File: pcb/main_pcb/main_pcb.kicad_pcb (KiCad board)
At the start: 2 copper layers, 80 x 100 mm, 58 parts, among them J1 Conn_01x05, J10 Conn_01x06_Male, J11 Conn_01x04, J12 Screw_Terminal_01x02, J13 Conn_01x02_Male, J2 Conn_01x05, J3 Conn_01x05, J4 Conn_01x05, J5 Conn_01x05, J6 Conn_01x05, J7 Conn_01x04, J8 Conn_01x06_Male, J9 Conn_01x04, Q1 Q_PMOS_GDS, SW1 SW_SPDT, U1 LSM6DSO, U2 Teensy_4.1, U3 DRV8833, U4 LM1117-3.3, U5 TPIC74101

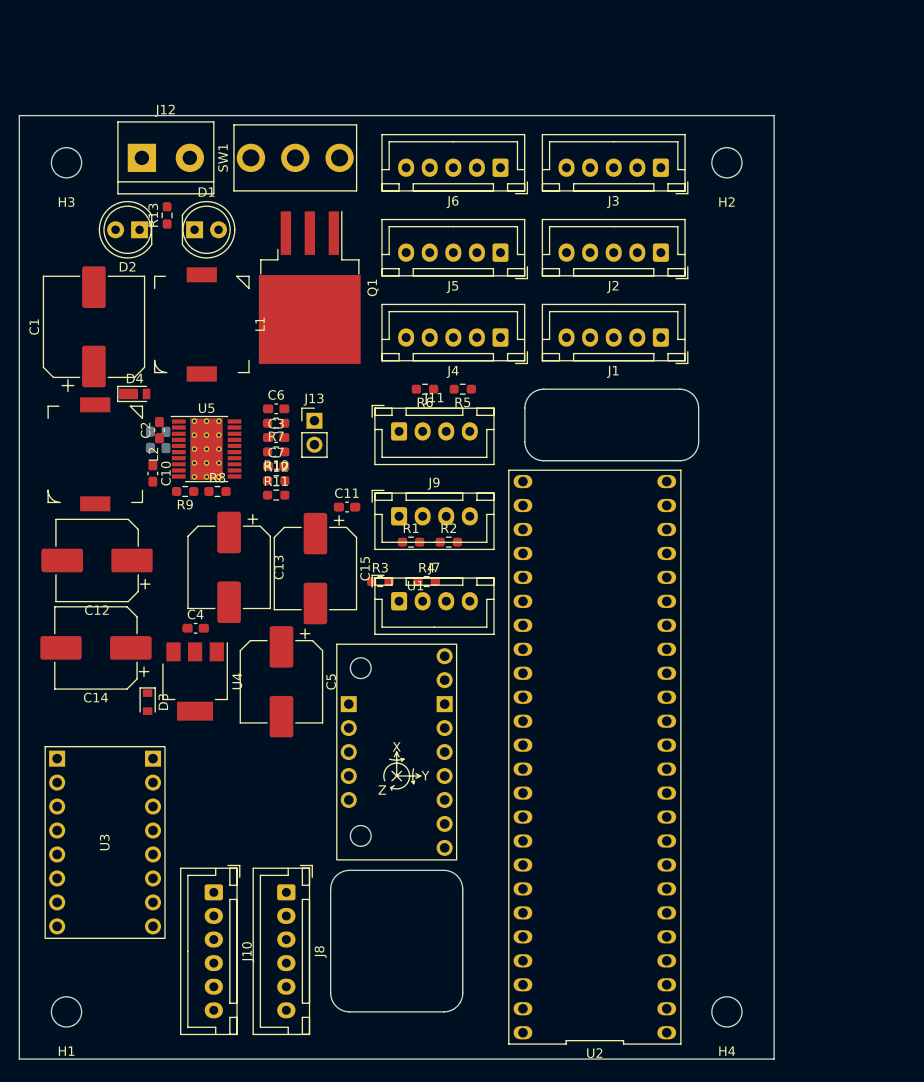
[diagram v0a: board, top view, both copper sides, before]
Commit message: Reorganize Teensy connections for optimized routing
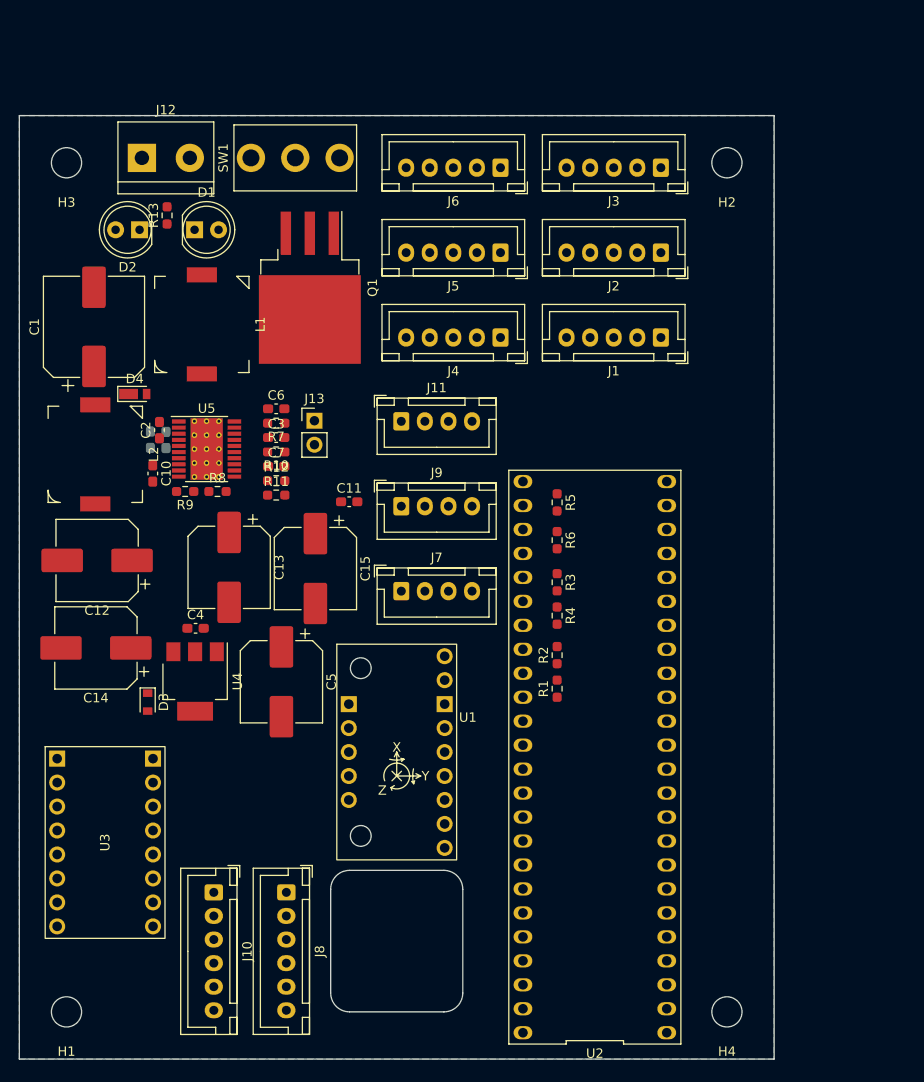
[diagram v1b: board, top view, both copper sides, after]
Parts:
- moved R1 21.9 mm to (107.0, 110.7), turned to 90 degrees
- moved R6 21.3 mm to (107.0, 95.0), turned to -90 degrees
- moved R3 18.7 mm to (107.0, 99.5), turned to -90 degrees
- moved R2 16.6 mm to (107.0, 107.2), turned to 90 degrees
- moved R5 15.6 mm to (107.0, 91.0), turned to -90 degrees
- moved R4 14.3 mm to (107.0, 103.0), turned to -90 degrees
- moved J11 1.09 mm to (90.5, 82.4)
- moved J7 1.09 mm to (90.5, 100.4)
- moved J9 1.09 mm to (90.5, 91.4)
- moved C11 0.60 mm to (85.0, 90.9)
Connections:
- net Net-(J2-Pad4) renamed /microcontroller/LCS2
- net Net-(J5-Pad4) renamed /microcontroller/LCS5
- J1 pad 2: /microcontroller/SDA -> /microcontroller/SDA2
- J1 pad 3: /microcontroller/SCL -> /microcontroller/SCL2
- J1 pad 4: Net-(J1-Pad4) -> /microcontroller/LCS1
- J2 pad 2: /microcontroller/SDA -> /microcontroller/SDA2
- J2 pad 3: /microcontroller/SCL -> /microcontroller/SCL2
- J3 pad 2: /microcontroller/SDA -> /microcontroller/SDA2
- J3 pad 3: /microcontroller/SCL -> /microcontroller/SCL2
- J3 pad 4: Net-(J3-Pad4) -> /microcontroller/LCS3
- J4 pad 2: /microcontroller/SDA -> /microcontroller/SDA2
- J4 pad 3: /microcontroller/SCL -> /microcontroller/SCL2
- J4 pad 4: Net-(J4-Pad4) -> /microcontroller/LCS4
- J5 pad 2: /microcontroller/SDA -> /microcontroller/SDA2
- J5 pad 3: /microcontroller/SCL -> /microcontroller/SCL2
- J6 pad 2: /microcontroller/SDA -> /microcontroller/SDA2
- J6 pad 3: /microcontroller/SCL -> /microcontroller/SCL2
- J6 pad 4: Net-(J6-Pad4) -> /microcontroller/LCS6
- U1 pad 10: /microcontroller/SCL -> /microcontroller/SCL1
- U1 pad 11: /microcontroller/SDA -> /microcontroller/SDA1
- U2 pad 11: Net-(J4-Pad4) -> /microcontroller/LCS6
- U2 pad 12: Net-(J3-Pad4) -> /microcontroller/LCS1
- U2 pad 14: Net-(J1-Pad4) -> /microcontroller/LCS3
- U2 pad 16: Net-(U2-Pad16) -> /microcontroller/SCL2
- U2 pad 17: Net-(U2-Pad17) -> /microcontroller/SDA2
- U2 pad 18: /microcontroller/AEQ2 -> unconnected-(U2-Pad18)
- U2 pad 19: /microcontroller/AEQ1 -> unconnected-(U2-Pad19)
- U2 pad 20: Net-(U2-Pad20) -> unconnected-(U2-Pad20)
- U2 pad 21: Net-(U2-Pad21) -> unconnected-(U2-Pad21)
- U2 pad 22: /microcontroller/BEQ2 -> unconnected-(U2-Pad22)
- U2 pad 23: /microcontroller/BEQ1 -> unconnected-(U2-Pad23)
- U2 pad 28: /microcontroller/Trig1 -> /microcontroller/Trig3
- U2 pad 29: /microcontroller/Echo1 -> /microcontroller/Echo3
- U2 pad 3: unconnected-(U2-Pad3) -> /microcontroller/BEQ1
- U2 pad 32: /microcontroller/Trig3 -> /microcontroller/Trig1
- U2 pad 33: /microcontroller/Echo3 -> /microcontroller/Echo1
- U2 pad 38: /microcontroller/SCL -> /microcontroller/SCL1
- U2 pad 39: /microcontroller/SDA -> /microcontroller/SDA1
- U2 pad 4: unconnected-(U2-Pad4) -> /microcontroller/BEQ2
- U2 pad 40: unconnected-(U2-Pad40) -> /microcontroller/BIN1
- U2 pad 41: unconnected-(U2-Pad41) -> /microcontroller/AIN2
- U2 pad 44: unconnected-(U2-Pad44) -> /microcontroller/AEQ2
- U2 pad 45: unconnected-(U2-Pad45) -> /microcontroller/AEQ1
- U2 pad 5: unconnected-(U2-Pad5) -> /microcontroller/AIN1
- U2 pad 6: unconnected-(U2-Pad6) -> /microcontroller/BIN2
- U2 pad 9: Net-(J6-Pad4) -> /microcontroller/LCS1
- U3 pad 11: Net-(U2-Pad16) -> /microcontroller/AIN1
- U3 pad 12: Net-(U2-Pad17) -> /microcontroller/AIN2
- U3 pad 13: Net-(U2-Pad20) -> /microcontroller/BIN2
- U3 pad 14: Net-(U2-Pad21) -> /microcontroller/BIN1
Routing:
- added copper zone on B.Cu, net GND
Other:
- outline, holes or cut-outs redrawn
- board text added: "TODO: * Add Micromouse * Add designers' names * Add Pololu logo * HWrev info"

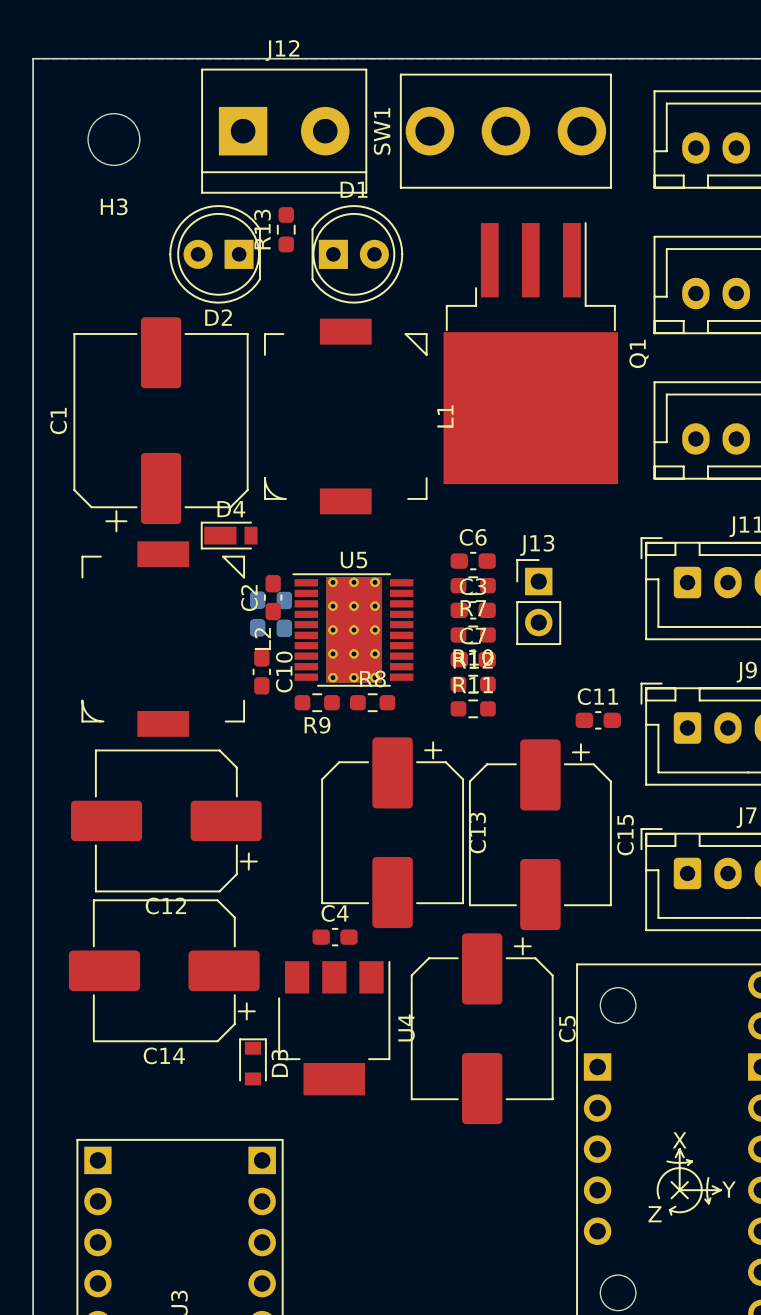
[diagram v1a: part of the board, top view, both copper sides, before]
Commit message: Set up design rules
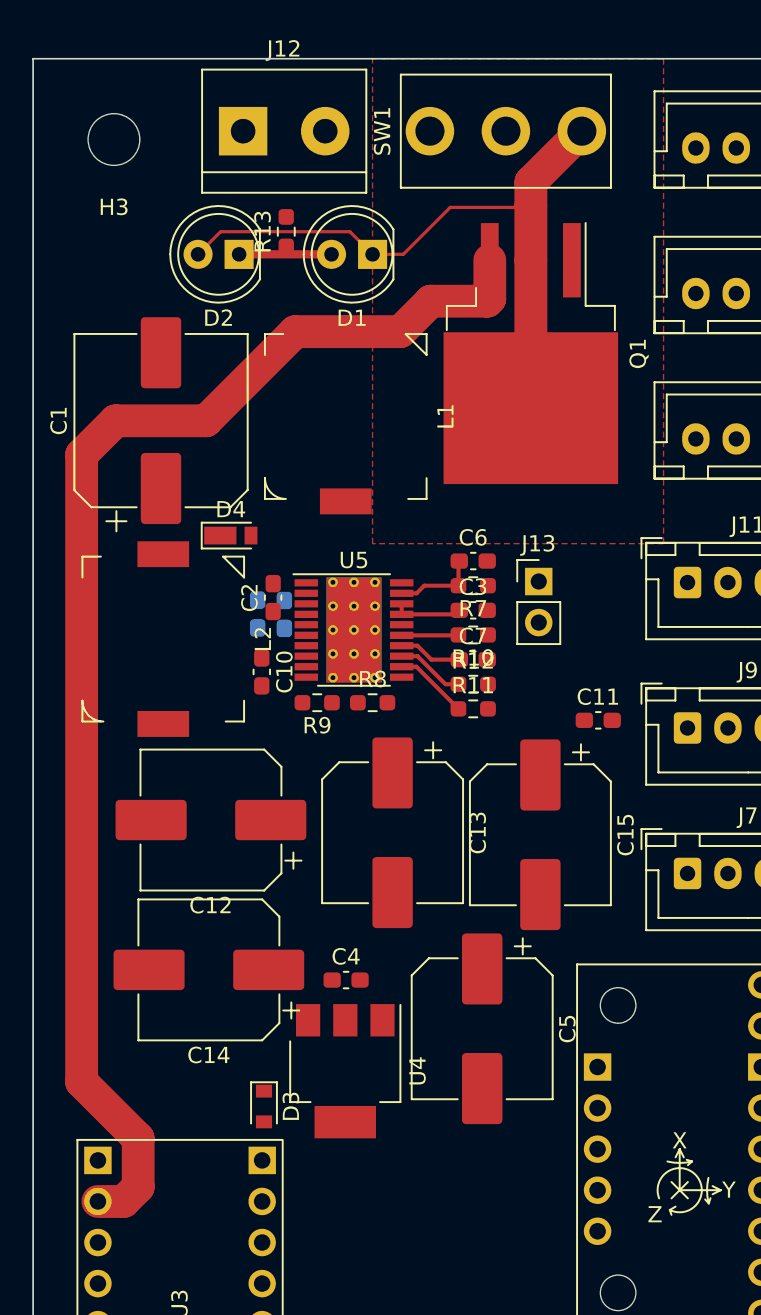
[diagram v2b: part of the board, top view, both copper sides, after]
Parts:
- moved C12 2.76 mm to (61.0, 97.1)
- moved C14 2.76 mm to (60.9, 106.4)
- moved U4 2.74 mm to (69.3, 112.6)
- moved D3 2.74 mm to (64.3, 114.8)
- moved C4 2.74 mm to (69.4, 107.0)
- moved D1 2.42 mm to (71.0, 62.1), turned to 180 degrees
- moved R13 0.12 mm to (65.7, 60.7)
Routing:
- net +BATT: track 0.00 -> 81.2 mm
- net Net-(D1-Pad1): track 0.00 -> 41.4 mm
- net Net-(D1-Pad2): track 0.00 -> 5.72 mm
- net Net-(C6-Pad1): track 0.00 -> 5.25 mm
- net Net-(R11-Pad1): track 0.00 -> 4.59 mm
- net Net-(C3-Pad1): track 0.00 -> 4.32 mm
- net Net-(R12-Pad1): track 0.00 -> 4.23 mm
- net Net-(C7-Pad1): track 0.00 -> 3.92 mm
- net Net-(R10-Pad2): track 0.00 -> 3.52 mm
- added copper zone on F.Cu, net Net-(D1-Pad1)
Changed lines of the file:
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@@
   )
   (setup
+    (stackup
+      (layer "F.SilkS" (type "Top Silk Screen"))
+      (layer "F.Paste" (type "Top Solder Paste"))
+      (layer "F.Mask" (type "Top Solder Mask") (thickness 0.01))
+      (layer "F.Cu" (type "copper") (thickness 0.035))
+      (layer "dielectric 1" (type "core") (thickness 1.51) (material "FR4") (epsilon_r 4.5) (loss_tangent 0.02))
+      (layer "B.Cu" (type "copper") (thickness 0.035))
+      (layer "B.Mask" (type "Bottom Solder Mask") (thickness 0.01))
+      (layer "B.Paste" (type "Bottom Solder Paste"))
+      (layer "B.SilkS" (type "Bottom Silk Screen"))
+      (copper_finish "None")
+      (dielectric_constraints no)
+    )
     (pad_to_mask_clearance 0)
     (pcbplotparams
@@
   (net 85 "/microcontroller/LCS6")
   (footprint "LED_THT:LED_D5.0mm" (layer "F.Cu")
-    (at 68.575 62.103)
+    (at 71 62.103 180)
     (descr "LED, diameter 5.0mm, 2 pins, http://cdn-reichelt.de/documents/datenblatt/A500/LL-504BC2E-009.pdf")
     (tags "LED diameter 5.0mm 2 pins")
@@
     (fp_arc (start -1.23 -1.469694) (mid 4.17 0.000016) (end -1.230016 1.469666) (layer "F.Fab") (width 0.1))
     (fp_circle (center 1.27 0) (end 3.77 0) (layer "F.Fab") (width 0.1) (fill none))
-    (pad "1" thru_hole rect (at 0 0) (size 1.8 1.8) (drill 0.9) (layers *.Cu *.Mask)
+    (pad "1" thru_hole rect (at 0 0 180) (size 1.8 1.8) (drill 0.9) (layers *.Cu *.Mask)
       (net 13 "Net-(D1-Pad1)") (pinfunction "K") (pintype "passive"))
-    (pad "2" thru_hole circle (at 2.54 0) (size 1.8 1.8) (drill 0.9) (layers *.Cu *.Mask)
+    (pad "2" thru_hole circle (at 2.54 0 180) (size 1.8 1.8) (drill 0.9) (layers *.Cu *.Mask)
       (net 14 "Net-(D1-Pad2)") (pinfunction "A") (pintype "passive"))
     (model "${KICAD6_3DMODEL_DIR}/LED_THT.3dshapes/LED_D5.0mm.wrl"
@@
   )
   (footprint "Package_TO_SOT_SMD:SOT-223-3_TabPin2" (layer "F.Cu")
-    (at 68.6308 109.982 -90)
+    (at 69.3117 112.6388 -90)
     (descr "module CMS SOT223 4 pins")
     (tags "CMS SOT")
@@
   )
   (footprint "Capacitor_SMD:C_0603_1608Metric_Pad1.08x0.95mm_HandSolder" (layer "F.Cu")
-    (at 68.6816 104.3432)
+    (at 69.3625 107)
     (descr "Capacitor SMD 0603 (1608 Metric), square (rectangular) end terminal, IPC_7351 nominal with elongated pad for handsoldering. (Body size source: IPC-SM-782 page 76, https://www.pcb-3d.com/wordpress/wp-content/uploads/ipc-sm-782a_amendment_1_and_2.pdf), generated with kicad-footprint-generator")
     (tags "capacitor handsolder")
@@
   )
   (footprint "Capacitor_SMD:CP_Elec_8x10.5" (layer "F.Cu")
-    (at 58.2422 97.155 180)
+    (at 61 97.1 180)
     (descr "SMD capacitor, aluminum electrolytic, Vishay 0810, 8.0x10.5mm, http://www.vishay.com/docs/28395/150crz.pdf")
     (tags "capacitor electrolytic")
@@
   )
   (footprint "Diode_SMD:D_SOD-110" (layer "F.Cu")
-    (at 63.6016 112.1664 -90)
+    (at 64.2825 114.8232 -90)
     (descr "SOD-110")
     (tags "SOD-110")
@@
   )
   (footprint "Resistor_SMD:R_0603_1608Metric_Pad0.98x0.95mm_HandSolder" (layer "F.Cu")
-    (at 65.659 60.579 90)
+    (at 65.659 60.7 90)
     (descr "Resistor SMD 0603 (1608 Metric), square (rectangular) end terminal, IPC_7351 nominal with elongated pad for handsoldering. (Body size source: IPC-SM-782 page 72, https://www.pcb-3d.com/wordpress/wp-content/uploads/ipc-sm-782a_amendment_1_and_2.pdf), generated with kicad-footprint-generator")
     (tags "resistor handsolder")
@@
   )
   (footprint "Capacitor_SMD:CP_Elec_8x10.5" (layer "F.Cu")
-    (at 58.1152 106.426 180)
+    (at 60.873 106.371 180)
     (descr "SMD capacitor, aluminum electrolytic, Vishay 0810, 8.0x10.5mm, http://www.vishay.com/docs/28395/150crz.pdf")
     (tags "capacitor electrolytic")
@@
     (effects (font (size 3 3) (thickness 0.6)) (justify left))
   )
+  (segment (start 76.117 84.374) (end 76.3645 84.1265) (width 0.254) (layer "F.Cu") (net 3))
+  (segment (start 72.8 83.724) (end 72.8 84.374) (width 0.254) (layer "F.Cu") (net 3))
+  (segment (start 72.8 84.374) (end 76.117 84.374) (width 0.254) (layer "F.Cu") (net 3))
+  (segment (start 76.3145 81.1285) (end 76.3645 81.0785) (width 0.254) (layer "F.Cu") (net 5))
+  (segment (start 72.8 83.074) (end 73.725 83.074) (width 0.254) (layer "F.Cu") (net 5))
+  (segment (start 76.3145 82.6025) (end 76.3145 81.1285) (width 0.254) (layer "F.Cu") (net 5))
+  (segment (start 74.1965 82.6025) (end 76.3145 82.6025) (width 0.254) (layer "F.Cu") (net 5))
+  (segment (start 73.725 83.074) (end 74.1965 82.6025) (width 0.254) (layer "F.Cu") (net 5))
+  (segment (start 74.6395 87.1745) (end 76.3645 87.1745) (width 0.254) (layer "F.Cu") (net 6))
+  (segment (start 73.779 86.314) (end 74.6395 87.1745) (width 0.254) (layer "F.Cu") (net 6))
+  (segment (start 72.8 86.314) (end 73.779 86.314) (width 0.254) (layer "F.Cu") (net 6))
+  (segment (start 60.203 62.103) (end 61.606 60.7) (width 0.2) (layer "F.Cu") (net 13))
+  (segment (start 69.597 60.7) (end 71 62.103) (width 0.2) (layer "F.Cu") (net 13))
+  (segment (start 80.791 62.466) (end 80.791 59.109) (width 2.032) (layer "F.Cu") (net 13))
+  (segment (start 71 62.103) (end 72.897 62.103) (width 0.2) (layer "F.Cu") (net 13))
+  (segment (start 80.791 59.109) (end 80.791 57.64) (width 2.032) (layer "F.Cu") (net 13))
+  (segment (start 80.791 57.64) (end 83.948 54.483) (width 2.032) (layer "F.Cu") (net 13))
+  (segment (start 75.8 59.2) (end 80.7 59.2) (width 0.2) (layer "F.Cu") (net 13))
+  (segment (start 72.897 62.103) (end 75.8 59.2) (width 0.2) (layer "F.Cu") (net 13))
+  (segment (start 61.606 60.7) (end 69.597 60.7) (width 0.2) (layer "F.Cu") (net 13))
+  (segment (start 80.791 62.466) (end 80.791 71.616) (width 2.032) (layer "F.Cu") (net 13))
+  (segment (start 80.7 59.2) (end 80.791 59.109) (width 0.2) (layer "F.Cu") (net 13))
+  (segment (start 62.743 62.103) (end 68.46 62.103) (width 0.508) (layer "F.Cu") (net 14))
+  (segment (start 54.009 120.697) (end 55.601 120.697) (width 2.032) (layer "F.Cu") (net 30))
+  (segment (start 56.5 119.798) (end 56.5 116.8) (width 2.032) (layer "F.Cu") (net 30))
+  (segment (start 78.251 64.849) (end 78.251 62.466) (width 2.032) (layer "F.Cu") (net 30))
+  (segment (start 74.6 65) (end 78.1 65) (width 2.032) (layer "F.Cu") (net 30))
+  (segment (start 53 113.3) (end 53 74.5) (width 2.032) (layer "F.Cu") (net 30))
+  (segment (start 72.714 66.886) (end 74.6 65) (width 2.032) (layer "F.Cu") (net 30))
+  (segment (start 56.5 116.8) (end 53 113.3) (width 2.032) (layer "F.Cu") (net 30))
+  (segment (start 60.7 72.4) (end 66.214 66.886) (width 2.032) (layer "F.Cu") (net 30))
+  (segment (start 55.601 120.697) (end 56.5 119.798) (width 2.032) (layer "F.Cu") (net 30))
+  (segment (start 69.342 66.886) (end 72.714 66.886) (width 2.032) (layer "F.Cu") (net 30))
+  (segment (start 66.214 66.886) (end 69.342 66.886) (width 2.032) (layer "F.Cu") (net 30))
+  (segment (start 78.1 65) (end 78.251 64.849) (width 2.032) (layer "F.Cu") (net 30))
+  (segment (start 55.1 72.4) (end 60.7 72.4) (width 2.032) (layer "F.Cu") (net 30))
+  (segment (start 53 74.5) (end 55.1 72.4) (width 2.032) (layer "F.Cu") (net 30))
+  (segment (start 72.8 85.674) (end 76.291 85.674) (width 0.254) (layer "F.Cu") (net 35))
+  (segment (start 76.291 85.674) (end 76.3145 85.6505) (width 0.254) (layer "F.Cu") (net 35))
+  (segment (start 73.706 87.614) (end 76.3145 90.2225) (width 0.254) (layer "F.Cu") (net 36))
+  (segment (start 72.8 87.614) (end 73.706 87.614) (width 0.254) (layer "F.Cu") (net 36))
+  (segment (start 73.779 86.964) (end 75.5135 88.6985) (width 0.254) (layer "F.Cu") (net 37))
+  (segment (start 72.8 86.964) (end 73.779 86.964) (width 0.254) (layer "F.Cu") (net 37))
+  (segment (start 75.5135 88.6985) (end 76.3145 88.6985) (width 0.254) (layer "F.Cu") (net 37))
+  (zone (net 13) (net_name "Net-(D1-Pad1)") (layer "F.Cu") (hatch edge 0.508)
+    (priority 1)
+    (connect_pads thru_hole_only (clearance 0.508))
+    (min_thickness 0.254) (filled_areas_thickness no)
+    (fill yes (thermal_gap 0.508) (thermal_bridge_width 0.508))
+    (polygon
+      (pts
+        (xy 89 80)
+        (xy 71 80)
+        (xy 71 50)
+        (xy 85 50)
+        (xy 89 50)
+        (xy 89 60)
+      )
+    )
+  )
   (zone locked (net 2) (net_name "GND") (layer "B.Cu") (hatch edge 0.508)
